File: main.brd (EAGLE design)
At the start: 50.8 x 50.8 mm, 55 parts, among them U1 SN65HVD10_D_8

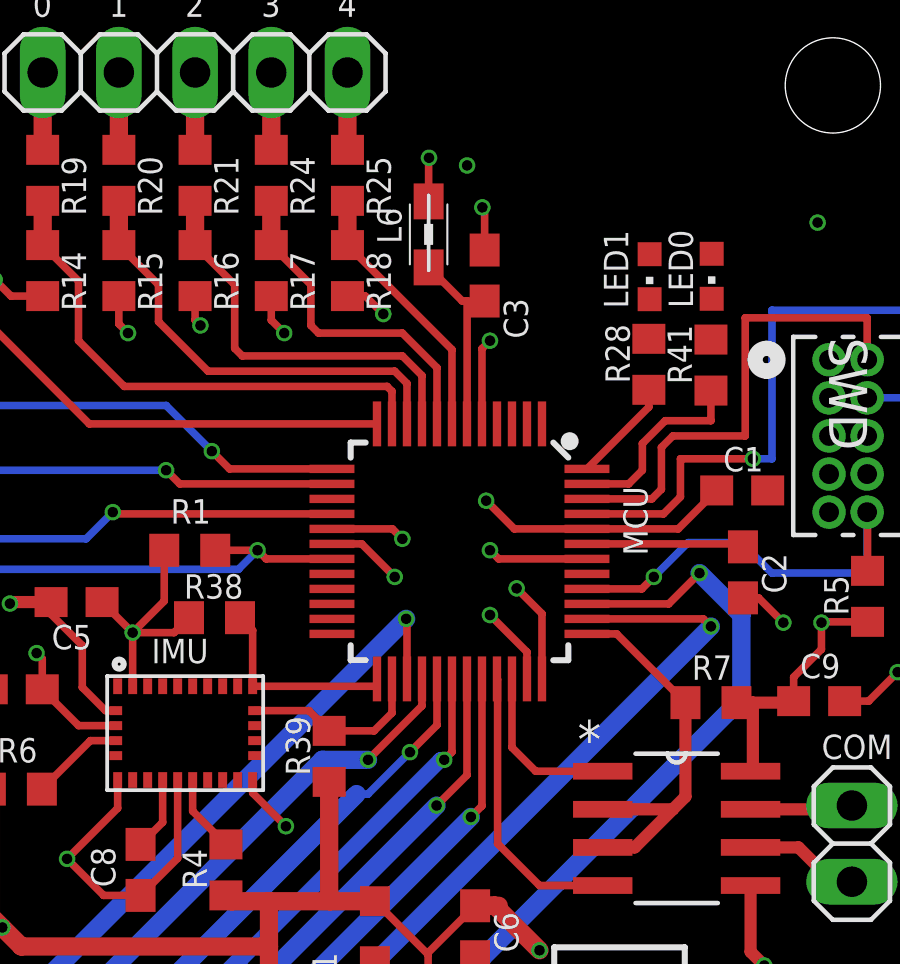
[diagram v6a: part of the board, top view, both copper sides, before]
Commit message: Added some traces, added a reset signal to IMU
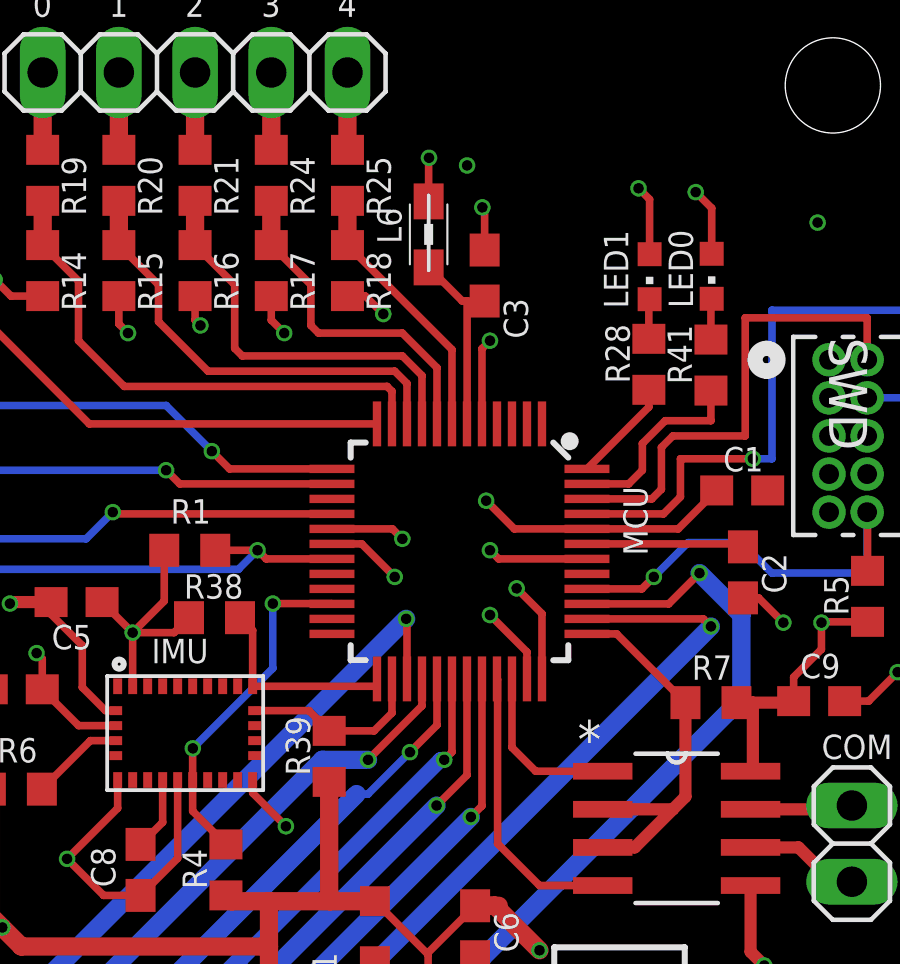
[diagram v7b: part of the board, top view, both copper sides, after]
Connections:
- removed net NRESET: IMU.11, R4.2
- new net IMU_NRST: IMU.11, MCU.22, R4.2
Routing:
- net IMU_NRST: track 0.00 -> 11.6 mm, vias 0 -> 2
- net 3.3V: track 97.7 -> 102.3 mm, vias 13 -> 15
- net NRESET: track 2.61 -> 0.00 mm
- net N$7: track 0.00 -> 1.37 mm
- net N$20: track 0.00 -> 1.33 mm
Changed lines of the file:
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@@
 <?xml version="1.0" encoding="utf-8"?>
 <!DOCTYPE eagle SYSTEM "eagle.dtd">
-<eagle version="8.7.1">
+<eagle version="9.0.0">
 <drawing>
 <settings>
@@
 <wire x1="33.5153" y1="44.5643" x2="33.528" y2="44.577" width="0.254" layer="1"/>
 <via x="33.528" y="44.577" extent="1-16" drill="0.35"/>
-<wire x1="40.8813" y1="41.3646" x2="42.9514" y2="41.3773" width="0" layer="19" extent="1-1"/>
-<wire x1="33.5153" y1="43.1243" x2="40.8813" y2="41.3646" width="0" layer="19" extent="1-1"/>
-<wire x1="46.863" y1="37.846" x2="42.9514" y2="41.3773" width="0" layer="19" extent="1-1"/>
-<wire x1="43.1174" y1="33.4899" x2="46.863" y2="37.846" width="0" layer="19" extent="1-1"/>
-<wire x1="36.449" y1="30.226" x2="36.3721" y2="32.2079" width="0" layer="19" extent="1-1"/>
-<wire x1="32.639" y1="31.877" x2="35.433" y2="33.147" width="0" layer="19" extent="1-1"/>
-<wire x1="46.6353" y1="29.1093" x2="43.1174" y2="33.4899" width="0" layer="19" extent="1-1"/>
-<wire x1="25.5279" y1="29.2481" x2="30.294" y2="32.2079" width="0" layer="19" extent="1-1"/>
-<wire x1="23.0875" y1="25.65" x2="23.65" y2="26.9625" width="0" layer="19" extent="1-1"/>
-<wire x1="18.9239" y1="23.5331" x2="21.8471" y2="25.65" width="0" layer="19" extent="1-1"/>
-<wire x1="14.986" y1="20.955" x2="18.9239" y2="19.3031" width="0" layer="19" extent="1-1"/>
-<wire x1="8.636" y1="19.939" x2="13.208" y2="19.9" width="0" layer="19" extent="1-1"/>
-<wire x1="3.4671" y1="13.208" x2="8.636" y2="19.939" width="0" layer="19" extent="1-1"/>
-<wire x1="12.7" y1="43.434" x2="4.0196" y2="33.0644" width="0" layer="19" extent="1-1"/>
+<wire x1="40.8813" y1="41.3646" x2="40.8813" y2="43.1927" width="0.254" layer="1"/>
+<wire x1="40.8813" y1="43.1927" x2="40.513" y2="43.561" width="0.254" layer="1"/>
+<via x="40.513" y="43.561" extent="1-16" drill="0.35"/>
+<wire x1="42.9514" y1="41.3773" x2="42.9514" y2="42.9006" width="0.254" layer="1"/>
+<wire x1="42.9514" y1="42.9006" x2="42.418" y2="43.434" width="0.254" layer="1"/>
+<via x="42.418" y="43.434" extent="1-16" drill="0.35"/>
 </signal>
 <signal name="GND">
@@
 <wire x1="35.294" y1="38.215" x2="35.56" y2="38.481" width="0.254" layer="1"/>
 <via x="35.56" y="38.481" extent="1-16" drill="0.35"/>
-<wire x1="46.863" y1="36.576" x2="46.482" y2="42.418" width="0" layer="19" extent="1-1"/>
-<wire x1="46.863" y1="35.306" x2="46.863" y2="36.576" width="0" layer="19" extent="1-1"/>
-<wire x1="46.863" y1="32.766" x2="46.863" y2="35.306" width="0" layer="19" extent="1-1"/>
-<wire x1="44.8174" y1="33.4899" x2="46.863" y2="32.766" width="0" layer="19" extent="1-1"/>
-<wire x1="44.5126" y1="29.9094" x2="44.8174" y2="33.4899" width="0" layer="19" extent="1-1"/>
-<wire x1="47.3828" y1="26.4668" x2="45.339" y2="29.083" width="0" layer="19" extent="1-1"/>
-<wire x1="38.794" y1="31.2079" x2="43.9928" y2="29.9094" width="0" layer="19" extent="1-1"/>
-<wire x1="35.56" y1="29.337" x2="35.8481" y2="31.2079" width="0" layer="19" extent="1-1"/>
-<wire x1="32.385" y1="30.607" x2="35.56" y2="31.496" width="0" layer="19" extent="1-1"/>
-<wire x1="35.294" y1="35.7079" x2="35.56" y2="31.496" width="0" layer="19" extent="1-1"/>
-<wire x1="35.3822" y1="41.5027" x2="35.56" y2="38.481" width="0" layer="19" extent="1-1"/>
-<wire x1="34.798" y1="44.323" x2="35.306" y2="42.926" width="0" layer="19" extent="1-1"/>
-<wire x1="32.004" y1="39.37" x2="35.294" y2="38.215" width="0" layer="19" extent="1-1"/>
-<wire x1="28.702" y1="38.735" x2="30.8102" y2="39.9678" width="0" layer="19" extent="1-1"/>
-<wire x1="25.908" y1="38.989" x2="28.2702" y2="39.1668" width="0" layer="19" extent="1-1"/>
-<wire x1="23.495" y1="38.735" x2="25.7302" y2="39.1668" width="0" layer="19" extent="1-1"/>
-<wire x1="20.6502" y1="39.9678" x2="23.1902" y2="39.9678" width="0" layer="19" extent="1-1"/>
-<wire x1="17.6406" y1="37.6044" x2="19.5952" y2="39.9678" width="0" layer="19" extent="1-1"/>
-<wire x1="17.653" y1="33.02" x2="18.034" y2="37.211" width="0" layer="19" extent="1-1"/>
-<wire x1="16.891" y1="29.845" x2="17.653" y2="33.02" width="0" layer="19" extent="1-1"/>
-<wire x1="18.923" y1="28.321" x2="16.8148" y2="29.7688" width="0" layer="19" extent="1-1"/>
-<wire x1="19.558" y1="29.718" x2="18.923" y2="28.321" width="0" layer="19" extent="1-1"/>
-<wire x1="23.0875" y1="24.65" x2="23.0875" y2="26.15" width="0" layer="19" extent="1-1"/>
-<wire x1="23.15" y1="23.8375" x2="23.0875" y2="24.65" width="0" layer="19" extent="1-1"/>
-<wire x1="25.15" y1="26.9625" x2="23.0875" y2="26.15" width="0" layer="19" extent="1-1"/>
-<wire x1="27.65" y1="23.8375" x2="25.15" y2="23.8375" width="0" layer="19" extent="1-1"/>
-<wire x1="27.7125" y1="24.65" x2="27.65" y2="23.8375" width="0" layer="19" extent="1-1"/>
-<wire x1="27.7125" y1="25.15" x2="27.7125" y2="24.65" width="0" layer="19" extent="1-1"/>
-<wire x1="27.7125" y1="25.65" x2="27.7125" y2="25.15" width="0" layer="19" extent="1-1"/>
-<wire x1="14.9268" y1="25.5194" x2="18.9366" y2="26.8605" width="0" layer="19" extent="1-1"/>
-<wire x1="16.256" y1="18.542" x2="14.351" y2="23.368" width="0" layer="19" extent="1-1"/>
-<wire x1="9.2955" y1="22.225" x2="14.351" y2="23.368" width="0" layer="19" extent="1-1"/>
-<wire x1="4.572" y1="22.606" x2="9.2955" y2="22.225" width="0" layer="19" extent="1-1"/>
-<wire x1="4.445" y1="20.066" x2="4.572" y2="22.606" width="0" layer="19" extent="1-1"/>
-<wire x1="3.4671" y1="15.748" x2="4.445" y2="20.066" width="0" layer="19" extent="1-1"/>
-<wire x1="6.985" y1="14.478" x2="3.4671" y2="15.748" width="0" layer="19" extent="1-1"/>
-<wire x1="7.112" y1="9.398" x2="6.985" y2="14.478" width="0" layer="19" extent="1-1"/>
-<wire x1="3.302" y1="8.636" x2="7.112" y2="9.398" width="0" layer="19" extent="1-1"/>
-<wire x1="8.128" y1="5.334" x2="7.112" y2="9.398" width="0" layer="19" extent="1-1"/>
-<wire x1="11.43" y1="3.302" x2="8.128" y2="5.334" width="0" layer="19" extent="1-1"/>
-<wire x1="44.2468" y1="20.32" x2="47.3828" y2="26.4668" width="0" layer="19" extent="1-1"/>
-<wire x1="47.244" y1="13.589" x2="44.704" y2="17.653" width="0" layer="19" extent="1-1"/>
-<wire x1="35.0647" y1="17.946" x2="28.758415625" y2="22.295584375" width="0" layer="19" extent="1-1"/>
-<wire x1="33.248596875" y1="14.6431" x2="33.9986" y2="15.5931" width="0" layer="19" extent="1-1"/>
-<wire x1="32.4986" y1="13.6931" x2="33.248596875" y2="14.6431" width="0" layer="19" extent="1-1"/>
-<wire x1="33.2486" y1="9.945" x2="31.369" y2="11.049" width="0" layer="19" extent="1-1"/>
-<wire x1="32.639" y1="5.842" x2="34.036" y2="7.747" width="0" layer="19" extent="1-1"/>
-<wire x1="35.9918" y1="3.3528" x2="32.639" y2="5.842" width="0" layer="19" extent="1-1"/>
-<wire x1="43.053" y1="3.937" x2="35.9918" y2="3.3528" width="0" layer="19" extent="1-1"/>
-<wire x1="2.9668" y1="35.2644" x2="3.5968" y2="25.4194" width="0" layer="19" extent="1-1"/>
-<wire x1="3.8518" y1="39.4044" x2="2.9668" y2="35.2644" width="0" layer="19" extent="1-1"/>
-<wire x1="10.033" y1="46.355" x2="5.5968" y2="39.4044" width="0" layer="19" extent="1-1"/>
 </signal>
 <signal name="VDDCORE">
@@
 <contactref element="LED1" pad="C"/>
 <contactref element="R28" pad="2"/>
-<wire x1="40.8559" y1="38.5436" x2="40.8813" y2="39.8646" width="0" layer="19" extent="1-1"/>
+<wire x1="40.8559" y1="38.5436" x2="40.8559" y2="39.8392" width="0.254" layer="1"/>
+<wire x1="40.8559" y1="39.8392" x2="40.8813" y2="39.8646" width="0.254" layer="1"/>
 </signal>
 <signal name="SW">
@@
 <contactref element="LED0" pad="C"/>
 <contactref element="R41" pad="2"/>
-<wire x1="42.926" y1="38.5182" x2="42.9514" y2="39.8773" width="0" layer="19" extent="1-1"/>
+<wire x1="42.926" y1="38.5182" x2="42.926" y2="39.8519" width="0.254" layer="1"/>
+<wire x1="42.926" y1="39.8519" x2="42.9514" y2="39.8773" width="0.254" layer="1"/>
 </signal>
 <signal name="PA17_SER1_I2C_SCL">
@@
 <wire x1="27.65" y1="26.9625" x2="31.794" y2="26.9625" width="0.254" layer="1"/>
 <wire x1="31.794" y1="26.9625" x2="31.794" y2="27.2079" width="0.254" layer="1"/>
-</signal>
-<signal name="NRESET">
-<contactref element="IMU" pad="11"/>
-<contactref element="R4" pad="2"/>
-<wire x1="26.7589" y1="21.6907" x2="25.65" y2="22.7996" width="0.254" layer="1"/>
-<wire x1="25.65" y1="22.7996" x2="25.65" y2="23.8375" width="0.254" layer="1"/>
 </signal>
 <signal name="N$15">
@@
 <wire x1="40.8559" y1="36.2698" x2="40.8559" y2="36.8436" width="0.254" layer="1"/>
 </signal>
+<signal name="IMU_NRST">
+<contactref element="MCU" pad="22"/>
+<contactref element="IMU" pad="11"/>
+<contactref element="R4" pad="2"/>
+<wire x1="26.7589" y1="21.6907" x2="25.65" y2="22.7996" width="0.254" layer="1"/>
+<wire x1="25.65" y1="22.7996" x2="25.65" y2="23.8375" width="0.254" layer="1"/>
+<wire x1="25.65" y1="23.8375" x2="25.65" y2="24.888" width="0.254" layer="1"/>
+<wire x1="25.65" y1="24.888" x2="25.654" y2="24.892" width="0.254" layer="1"/>
+<via x="25.654" y="24.892" extent="1-16" drill="0.35"/>
+<wire x1="25.654" y1="24.892" x2="28.321" y2="27.559" width="0.254" layer="16"/>
+<wire x1="28.321" y1="27.559" x2="28.321" y2="29.718" width="0.254" layer="16"/>
+<via x="28.321" y="29.718" extent="1-16" drill="0.35"/>
+<wire x1="28.321" y1="29.718" x2="30.2839" y2="29.718" width="0.254" layer="1"/>
+<wire x1="30.2839" y1="29.718" x2="30.294" y2="29.7079" width="0.254" layer="1"/>
+</signal>
 </signals>

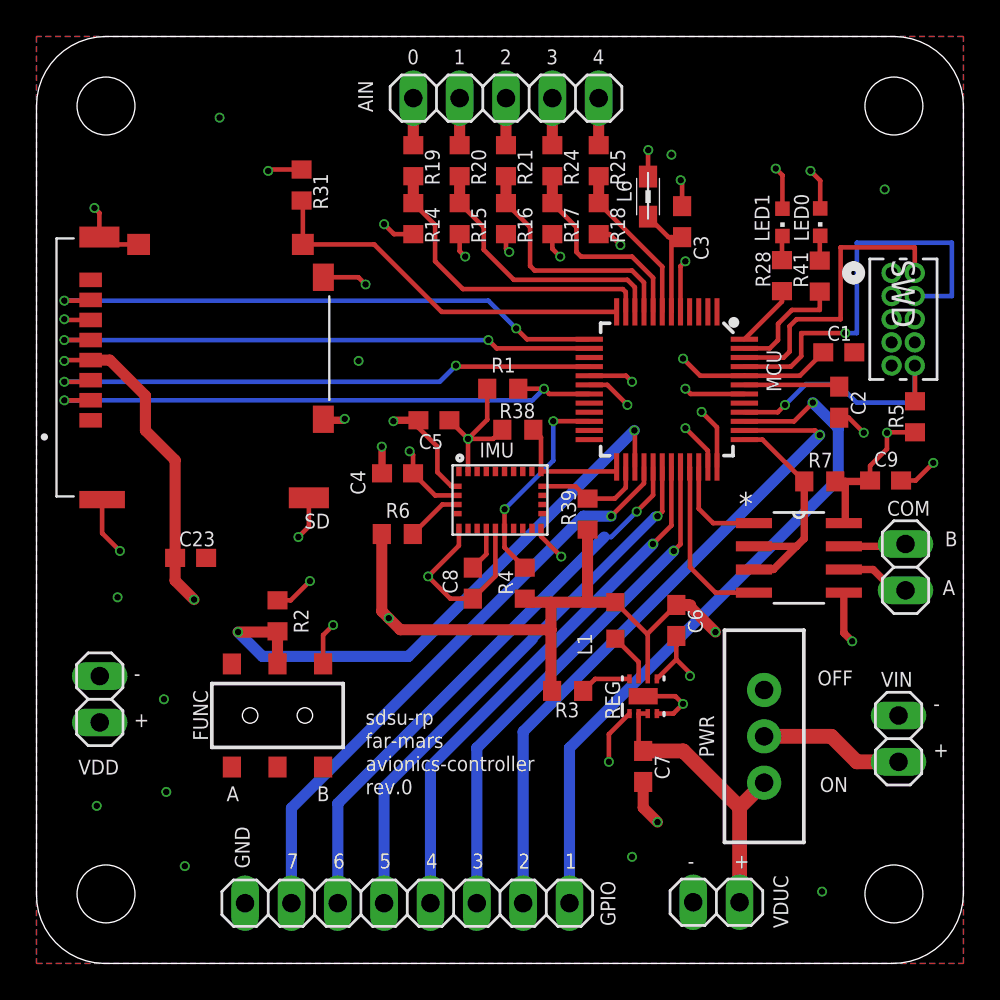
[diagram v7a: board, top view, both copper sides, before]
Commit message: Added Higned SD, rearranged silk
Added new hinged MicroSD for stability purposes, this sd card will be operating in a high g, high vibration enviornment and a spring ejection slot is not adequate. I also rearranged the labels on the silk screen as the headers were blocking a few. The SD card is also seated closer to the center, hopefully so the card no loner sticks out past the board dimensions.
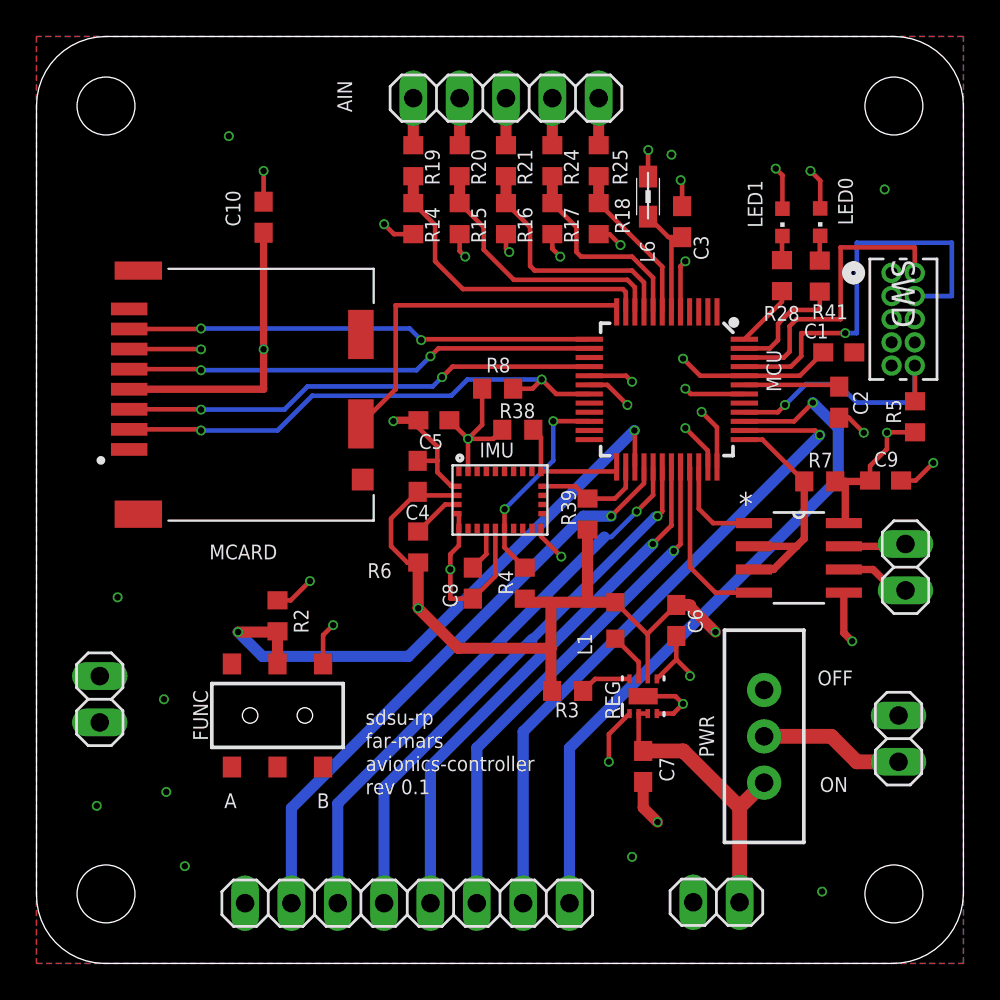
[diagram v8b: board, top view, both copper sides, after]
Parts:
- removed C23: 100n, resistor:C0603
- removed R1, R31: 10k, resistor:R0603
- removed SD: 503182-1852, molex-microSD:MOLEX_503182-1852
- added C10: 100n, resistor:C0603
- added MCARD: DM3CS-SF, DM3CS-SF:HRS_DM3CS-SF
- added R8: 10k, resistor:R0603
- moved R6 1.35 mm to (20.9, 22.8), turned to 90 degrees
- moved C4 1.12 mm to (20.9, 26.7), turned to 90 degrees
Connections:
- net 3.3V: now also C10.1, MCARD.4, R8.1; no longer C23.1, R1.1, R31.1, SD.4
- net GND: now also C10.2, MCARD.6, MCARD.S1, MCARD.S2, MCARD.S3, MCARD.S5; no longer C23.2, SD.6, SD.P1, SD.P2, SD.P3, SD.P4, SD.P5, SD.SW
- net SD_CD: now also MCARD.9; no longer R31.2, SD.DT
- net SD_CS: now also MCARD.2, R8.2; no longer R1.2, SD.2
- net SER0_P0_DI: now also MCARD.7; no longer SD.7
- net SER0_P1_CLK: now also MCARD.5; no longer SD.5
- net SER0_P3_DO: now also MCARD.3; no longer SD.3
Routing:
- net GND: track 77.8 -> 68.1 mm, vias 39 -> 33
- net SER0_P0_DI: track 31.1 -> 25.5 mm
- net SER0_P1_CLK: track 30.4 -> 25.7 mm
- net SER0_P3_DO: track 30.6 -> 26.2 mm
- net SD_CS: track 32.0 -> 28.5 mm
- net 3.3V: track 102.3 -> 99.0 mm, vias 15 -> 12
- net SD_CD: track 21.2 -> 19.8 mm
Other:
- board text added: "rev 0.1"
- board text removed: "rev.0"
